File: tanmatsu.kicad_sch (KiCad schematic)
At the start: 49 parts, among them J1 USB host, J10 External Add-On (SAO / PMOD), J2 Micro_SD_Card, J3 USB device, J4 Headphone, J5 Speaker, J6 CAMERA, J7 SAO, J8 Expansion I3C, J9 Internal Add-On, SW1 Boot, U1 USBLC6-2P6, U2 USBLC6-2P6, U3 CH334R, U4 USBLC6-2P6, U5 ESD, U6 ESD, Y1 12MHz

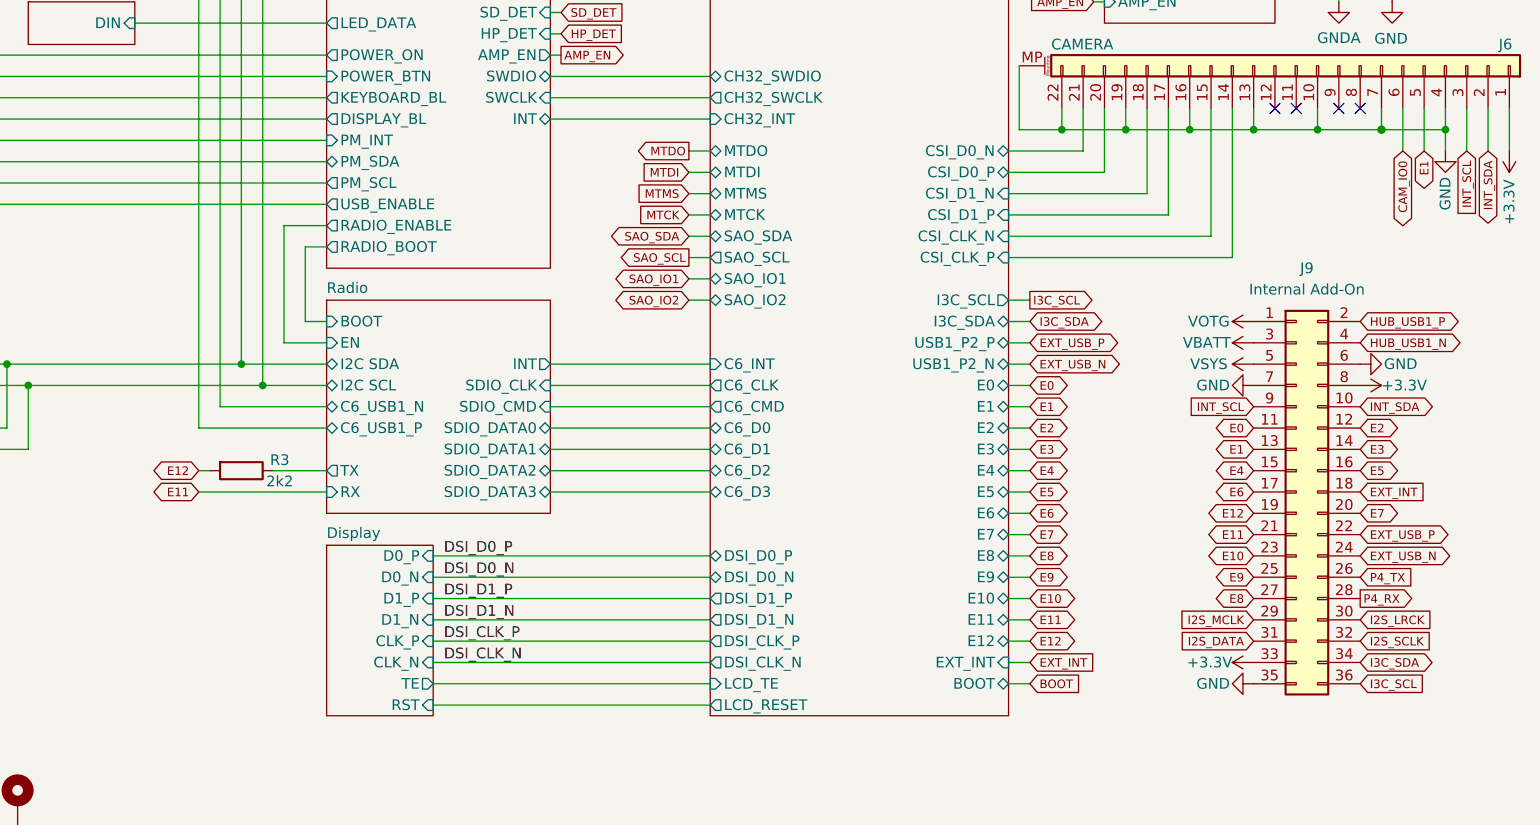
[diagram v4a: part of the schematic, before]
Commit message: Renumber add-on GPIOs
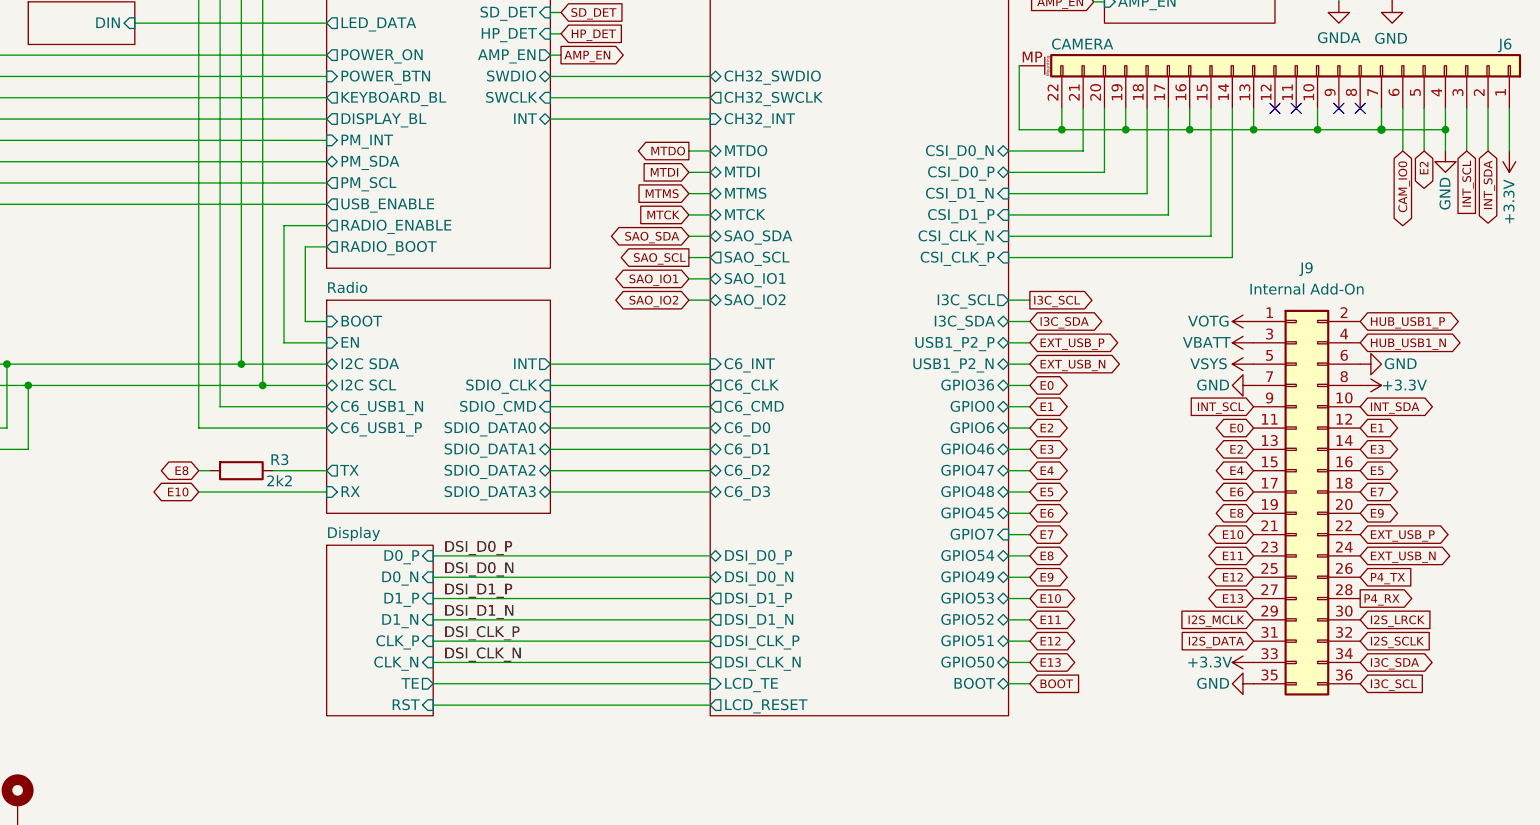
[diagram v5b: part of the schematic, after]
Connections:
- net EXT_INT is gone; now on net E7: J9.18 (Pin_18)
- net E1: now also J9.12 (Pin_12); no longer J6.5 (Pin_5), J9.13 (Pin_13)
- net E10: now also J9.21 (Pin_21); no longer J9.23 (Pin_23)
- net E11: now also J9.23 (Pin_23); no longer J9.21 (Pin_21)
- net E12: now also J9.25 (Pin_25); no longer J9.19 (Pin_19), R3.2
- net E2: now also J6.5 (Pin_5), J9.13 (Pin_13); no longer J9.12 (Pin_12)
- net E7: no longer J9.20 (Pin_20)
- net E8: now also J9.19 (Pin_19), R3.2; no longer J9.27 (Pin_27)
- net E9: now also J9.20 (Pin_20); no longer J9.25 (Pin_25)
- new net E13: J9.27 (Pin_27)
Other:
- sheet Application processor ports: added GPIO0, GPIO36, GPIO45, GPIO46, GPIO47, GPIO48, GPIO49, GPIO50, GPIO51, GPIO52, GPIO53, GPIO54, GPIO6, GPIO7; removed E0, E1, E10, E11, E12, E2, E3, E4, E5, E6, E7, E8, E9, EXT_INT
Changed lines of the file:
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@@
 	(wire
 		(pts
-			(xy 223.52 148.59) (xy 226.06 148.59)
+			(xy 223.52 156.21) (xy 226.06 156.21)
 		)
 		(stroke
@@
 	(wire
 		(pts
-			(xy 223.52 158.75) (xy 226.06 158.75)
+			(xy 223.52 143.51) (xy 226.06 143.51)
 		)
 		(stroke
@@
 	(wire
 		(pts
-			(xy 223.52 146.05) (xy 226.06 146.05)
+			(xy 223.52 158.75) (xy 226.06 158.75)
 		)
 		(stroke
@@
 	(wire
 		(pts
-			(xy 223.52 153.67) (xy 226.06 153.67)
+			(xy 223.52 151.13) (xy 226.06 151.13)
 		)
 		(stroke
@@
 	(wire
 		(pts
-			(xy 223.52 143.51) (xy 226.06 143.51)
+			(xy 223.52 148.59) (xy 226.06 148.59)
 		)
 		(stroke
@@
 	(wire
 		(pts
-			(xy 223.52 151.13) (xy 226.06 151.13)
+			(xy 223.52 153.67) (xy 226.06 153.67)
 		)
 		(stroke
@@
 	(wire
 		(pts
-			(xy 223.52 156.21) (xy 226.06 156.21)
+			(xy 223.52 146.05) (xy 226.06 146.05)
 		)
 		(stroke
@@
 	(global_label "E7"
 		(shape bidirectional)
-		(at 265.43 140.97 0)
+		(at 265.43 138.43 0)
 		(fields_autoplaced yes)
 		(effects
@@
 		)
 		(property "Intersheetrefs" "${INTERSHEET_REFS}"
-			(at 270.5937 140.97 0)
+			(at 270.5937 138.43 0)
 			(effects
 				(font
@@
 		)
 	)
+	(global_label "E2"
+		(shape bidirectional)
+		(at 273.05 97.79 270)
+		(fields_autoplaced yes)
+		(effects
+			(font
+				(size 1.016 1.016)
+			)
+			(justify right)
+		)
+		(property "Intersheetrefs" "${INTERSHEET_REFS}"
+			(at 273.05 102.9537 90)
+			(effects
+				(font
+					(size 1.27 1.27)
+				)
+				(justify right)
+				(hide yes)
+			)
+		)
+	)
 	(global_label "INT_SCL"
 		(shape input)
@@
 	(global_label "E2"
 		(shape bidirectional)
-		(at 265.43 130.81 0)
+		(at 252.73 133.35 180)
 		(fields_autoplaced yes)
 		(effects
@@
 				(size 1.016 1.016)
 			)
-			(justify left)
+			(justify right)
 		)
 		(property "Intersheetrefs" "${INTERSHEET_REFS}"
-			(at 270.5937 130.81 0)
+			(at 247.5663 133.35 0)
 			(effects
 				(font
 					(size 1.27 1.27)
 				)
-				(justify left)
+				(justify right)
 				(hide yes)
 			)
@@
 	(global_label "E12"
 		(shape bidirectional)
-		(at 252.73 140.97 180)
+		(at 252.73 148.59 180)
 		(fields_autoplaced yes)
 		(effects
@@
 		)
 		(property "Intersheetrefs" "${INTERSHEET_REFS}"
-			(at 246.5987 140.97 0)
+			(at 246.5987 148.59 0)
 			(effects
 				(font
@@
 		)
 	)
-	(global_label "E12"
-		(shape bidirectional)
-		(at 127 135.89 180)
-		(fields_autoplaced yes)
-		(effects
-			(font
-				(size 1.016 1.016)
-			)
-			(justify right)
-		)
-		(property "Intersheetrefs" "${INTERSHEET_REFS}"
-			(at 120.8687 135.89 0)
-			(effects
-				(font
-					(size 1.27 1.27)
-				)
-				(justify right)
-				(hide yes)
-			)
-		)
-	)
 	(global_label "MTMS"
 		(shape input)
@@
 	(global_label "E8"
 		(shape bidirectional)
-		(at 252.73 151.13 180)
+		(at 252.73 140.97 180)
+		(fields_autoplaced yes)
+		(effects
+			(font
+				(size 1.016 1.016)
+			)
+			(justify right)
+		)
+		(property "Intersheetrefs" "${INTERSHEET_REFS}"
+			(at 247.5663 140.97 0)
+			(effects
+				(font
+					(size 1.27 1.27)
+				)
+				(justify right)
+				(hide yes)
+			)
+		)
+	)
+	(global_label "E8"
+		(shape bidirectional)
+		(at 127 135.89 180)
 		(fields_autoplaced yes)
 		(effects
@@
 		)
 		(property "Intersheetrefs" "${INTERSHEET_REFS}"
-			(at 247.5663 151.13 0)
+			(at 121.8363 135.89 0)
 			(effects
 				(font
@@
 	(global_label "E10"
 		(shape bidirectional)
-		(at 252.73 146.05 180)
+		(at 252.73 143.51 180)
 		(fields_autoplaced yes)
 		(effects
@@
 		)
 		(property "Intersheetrefs" "${INTERSHEET_REFS}"
-			(at 246.5987 146.05 0)
+			(at 246.5987 143.51 0)
 			(effects
 				(font
@@
 	(global_label "E1"
 		(shape bidirectional)
-		(at 252.73 133.35 180)
+		(at 265.43 130.81 0)
 		(fields_autoplaced yes)
 		(effects
@@
 				(size 1.016 1.016)
 			)
-			(justify right)
+			(justify left)
 		)
 		(property "Intersheetrefs" "${INTERSHEET_REFS}"
-			(at 247.5663 133.35 0)
+			(at 270.5937 130.81 0)
 			(effects
 				(font
 					(size 1.27 1.27)
 				)
-				(justify right)
+				(justify left)
 				(hide yes)
 			)
 		)
 	)
-	(global_label "EXT_INT"
-		(shape input)
-		(at 265.43 138.43 0)
+	(global_label "E13"
+		(shape bidirectional)
+		(at 252.73 151.13 180)
 		(fields_autoplaced yes)
 		(effects
@@
 				(size 1.016 1.016)
 			)
-			(justify left)
+			(justify right)
 		)
 		(property "Intersheetrefs" "${INTERSHEET_REFS}"
-			(at 273.5752 138.43 0)
+			(at 246.5987 151.13 0)
 			(effects
 				(font
 					(size 1.27 1.27)
 				)
-				(justify left)
+				(justify right)
 				(hide yes)
 			)
@@
 		)
 	)
-	(global_label "E1"
-		(shape bidirectional)
-		(at 273.05 97.79 270)
-		(fields_autoplaced yes)
-		(effects
-			(font
-				(size 1.016 1.016)
-			)
-			(justify right)
-		)
-		(property "Intersheetrefs" "${INTERSHEET_REFS}"
-			(at 273.05 102.9537 90)
-			(effects
-				(font
-					(size 1.27 1.27)
-				)
-				(justify right)
-				(hide yes)
-			)
-		)
-	)
 	(global_label "SAO_SDA"
 		(shape output)
@@
 	(global_label "E11"
 		(shape bidirectional)
-		(at 252.73 143.51 180)
+		(at 252.73 146.05 180)
 		(fields_autoplaced yes)
 		(effects
@@
 		)
 		(property "Intersheetrefs" "${INTERSHEET_REFS}"
-			(at 246.5987 143.51 0)
+			(at 246.5987 146.05 0)
 			(effects
 				(font
@@
 	(global_label "E9"
 		(shape bidirectional)
-		(at 252.73 148.59 180)
+		(at 265.43 140.97 0)
 		(fields_autoplaced yes)
 		(effects
@@
 				(size 1.016 1.016)
 			)
-			(justify right)
+			(justify left)
 		)
 		(property "Intersheetrefs" "${INTERSHEET_REFS}"
-			(at 247.5663 148.59 0)
+			(at 270.5937 140.97 0)
 			(effects
 				(font
 					(size 1.27 1.27)
 				)
-				(justify right)
+				(justify left)
 				(hide yes)
 			)
@@
 		)
 	)
-	(global_label "E11"
+	(global_label "E10"
 		(shape bidirectional)
 		(at 127 138.43 180)
@@
 		)
 	)
-	(global_label "EXT_INT"
-		(shape input)
+	(global_label "E13"
+		(shape bidirectional)
 		(at 226.06 158.75 0)
 		(fields_autoplaced yes)
@@
 		)
 		(property "Intersheetrefs" "${INTERSHEET_REFS}"
-			(at 234.2052 158.75 0)
+			(at 232.1913 158.75 0)
 			(effects
 				(font
@@
 			)
 		)
-		(pin "EXT_INT" input
-			(at 223.52 158.75 0)
+		(pin "GPIO7" input
+			(at 223.52 143.51 0)
 			(effects
 				(font
@@
 			)
 		)
-		(pin "E2" bidirectional
-			(at 223.52 130.81 0)
+		(pin "BOOT" bidirectional
+			(at 223.52 161.29 0)
 			(effects
 				(font
@@
 			)
 		)
-		(pin "E0" bidirectional
+		(pin "GPIO36" bidirectional
 			(at 223.52 125.73 0)
 			(effects
@@
 			)
 		)
-		(pin "E6" bidirectional
-			(at 223.52 140.97 0)
+		(pin "GPIO6" bidirectional
+			(at 223.52 130.81 0)
 			(effects
 				(font
@@
 			)
 		)
-		(pin "E4" bidirectional
-			(at 223.52 135.89 0)
+		(pin "GPIO0" bidirectional
+			(at 223.52 128.27 0)
 			(effects
 				(font
@@
 			)
 		)
-		(pin "E3" bidirectional
+		(pin "GPIO46" bidirectional
 			(at 223.52 133.35 0)
 			(effects
@@
 			)
 		)
-		(pin "E5" bidirectional
-			(at 223.52 138.43 0)
+		(pin "GPIO47" bidirectional
+			(at 223.52 135.89 0)
 			(effects
 				(font
@@
 			)
 		)
-		(pin "BOOT" bidirectional
-			(at 223.52 161.29 0)
+		(pin "GPIO48" bidirectional
+			(at 223.52 138.43 0)
 			(effects
 				(font
@@
 			)
 		)
-		(pin "E1" bidirectional
-			(at 223.52 128.27 0)
+		(pin "GPIO45" bidirectional
+			(at 223.52 140.97 0)
 			(effects
 				(font
@@
 			)
 		)
-		(pin "E7" bidirectional
-			(at 223.52 143.51 0)
+		(pin "GPIO49" bidirectional
+			(at 223.52 148.59 0)
 			(effects
 				(font
@@
 			)
 		)
-		(pin "E10" bidirectional
-			(at 223.52 151.13 0)
+		(pin "GPIO52" bidirectional
+			(at 223.52 153.67 0)
 			(effects
 				(font
@@
 			)
 		)
-		(pin "E8" bidirectional
-			(at 223.52 146.05 0)
+		(pin "GPIO51" bidirectional
+			(at 223.52 156.21 0)
 			(effects
 				(font
@@
 			)
 		)
-		(pin "E9" bidirectional
-			(at 223.52 148.59 0)
+		(pin "GPIO53" bidirectional
+			(at 223.52 151.13 0)
 			(effects
 				(font
@@
 			)
 		)
-		(pin "E11" bidirectional
-			(at 223.52 153.67 0)
+		(pin "GPIO54" bidirectional
+			(at 223.52 146.05 0)
 			(effects
 				(font
@@
 			)
 		)
-		(pin "E12" bidirectional
-			(at 223.52 156.21 0)
+		(pin "GPIO50" bidirectional
+			(at 223.52 158.75 0)
 			(effects
 				(font
